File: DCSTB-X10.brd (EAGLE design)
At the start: 29 x 104 mm, 7 parts

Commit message: Fixed QR code on x8 and x10 board. Generated CAM files.
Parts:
- moved LOGO2 1.00 mm to (11.0, 1.00)
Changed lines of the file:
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@@
 <element name="U$4" library="KF8500-Terminals" package="KF8500-8.5-2P" value="KF8500-8.5-2P" x="15" y="69" smashed="yes" rot="R90"/>
 <element name="LOGO1" library="_my_logos" package="MFDEC_L_10MM" value="MFDECLOGO_L_10MM" x="15" y="92" smashed="yes" rot="MR0"/>
-<element name="LOGO2" library="_my_logos" package="RSNURL_QR_10MM" value="RSNURL_QR_10MM" x="10" y="1" smashed="yes" rot="MR0"/>
+<element name="LOGO2" library="_my_logos" package="RSNURL_QR_10MM" value="RSNURL_QR_10MM" x="11" y="1" smashed="yes" rot="MR0"/>
 <element name="U$5" library="KF8500-Terminals" package="KF8500-8.5-2P" value="KF8500-8.5-2P" x="15" y="86" smashed="yes" rot="R90"/>
 </elements>

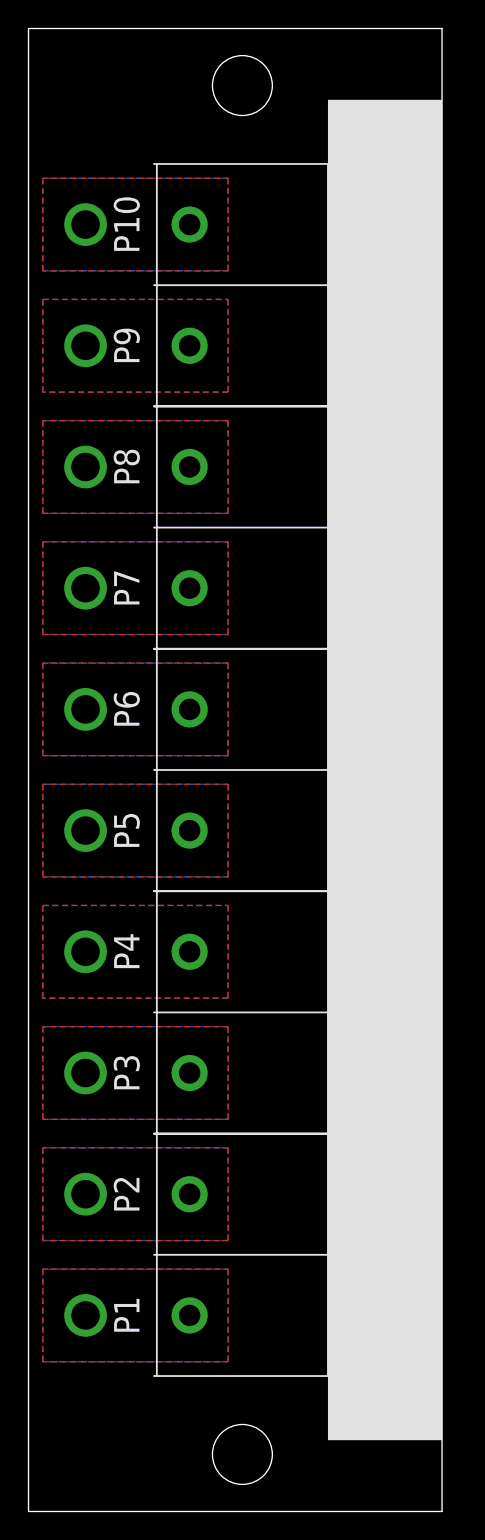
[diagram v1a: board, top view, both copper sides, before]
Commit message: Made boards a little bigger. Generated PNG preview. Generated CAM files.
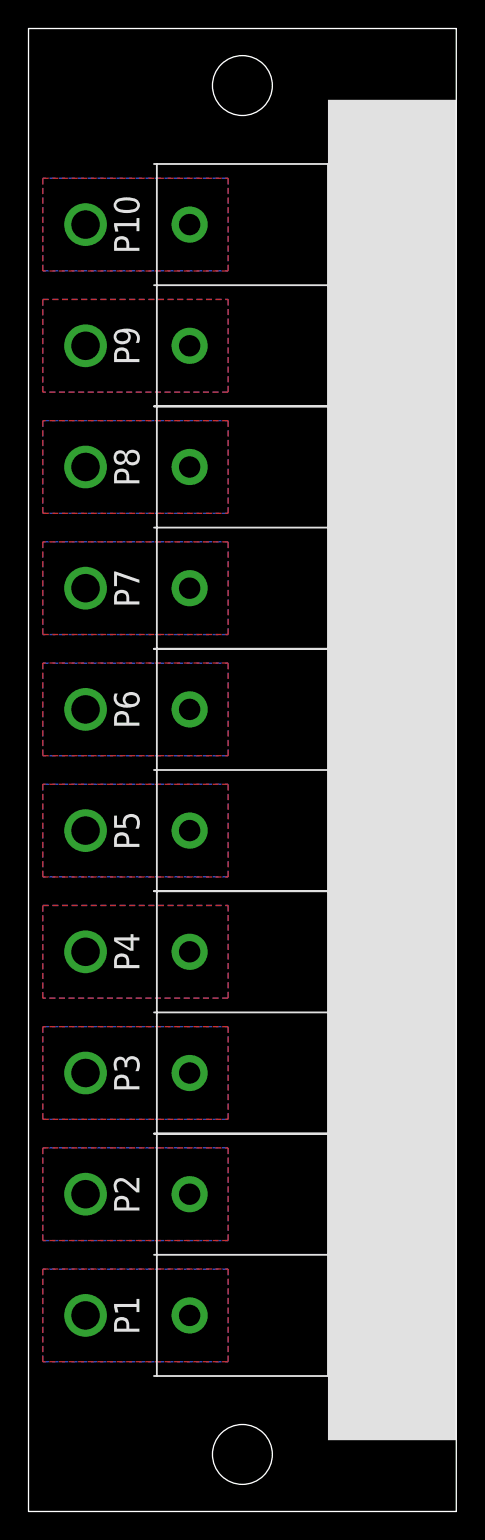
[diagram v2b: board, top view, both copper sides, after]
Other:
- board size 29 x 104 mm -> 30 x 104 mm
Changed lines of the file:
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@@
 <drawing>
 <settings>
-<setting alwaysvectorfont="yes"/>
+<setting alwaysvectorfont="no"/>
 <setting verticaltext="up"/>
 </settings>
@@
 <board>
 <plain>
-<wire x1="0" y1="0" x2="29" y2="0" width="0" layer="20"/>
-<wire x1="29" y1="0" x2="29" y2="104" width="0" layer="20"/>
-<wire x1="29" y1="104" x2="0" y2="104" width="0" layer="20"/>
+<wire x1="0" y1="0" x2="30" y2="0" width="0" layer="20"/>
+<wire x1="30" y1="0" x2="30" y2="104" width="0" layer="20"/>
+<wire x1="30" y1="104" x2="0" y2="104" width="0" layer="20"/>
 <wire x1="0" y1="104" x2="0" y2="0" width="0" layer="20"/>
 <hole x="15" y="4" drill="4.2"/>
@@
 <circle x="15" y="4" radius="4.5" width="0.127" layer="51"/>
 <circle x="15" y="100" radius="4.5" width="0.127" layer="51"/>
-<text x="28" y="63" size="1.778" layer="22" font="vector" rot="MR270">DCSTB-X10-0010
+<text x="29" y="63" size="1.778" layer="22" font="vector" rot="MR270">DCSTB-X10-0010
 (c) Andriy Golovnya
 http://redscorp.net</text>
-<rectangle x1="21" y1="5" x2="29" y2="99" layer="21"/>
+<rectangle x1="21" y1="5" x2="30" y2="99" layer="21"/>
 <text x="6" y="13.75" size="1.778" layer="21" font="vector" rot="R90" align="top-center">P1</text>
 <text x="6" y="22.25" size="1.778" layer="21" font="vector" rot="R90" align="top-center">P2</text>
